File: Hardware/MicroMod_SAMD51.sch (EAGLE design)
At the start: 17 parts, among them J2 MICROMOD-2222, U1 W25QXX6X5, U2 ATSAMD51J20A-A, Y1 32.768kHz

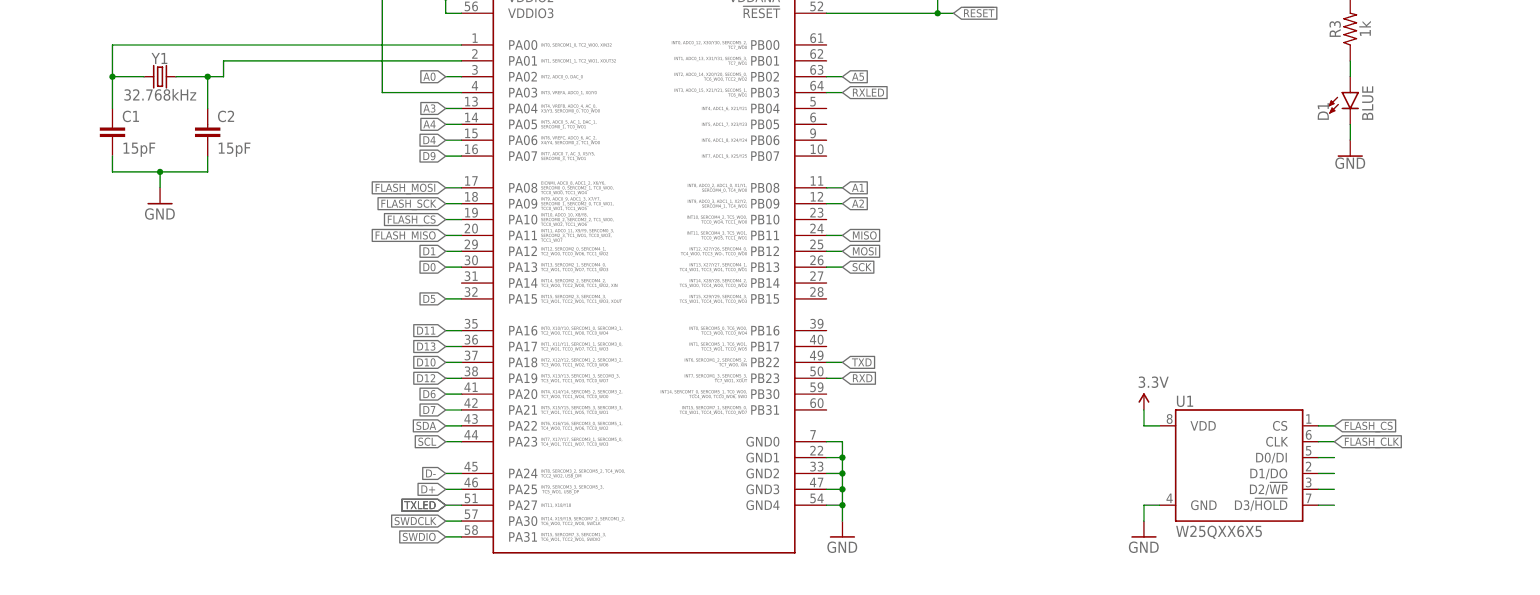
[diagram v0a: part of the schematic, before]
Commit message: Adds notes for quad spi, spi, and analog pins to schematic
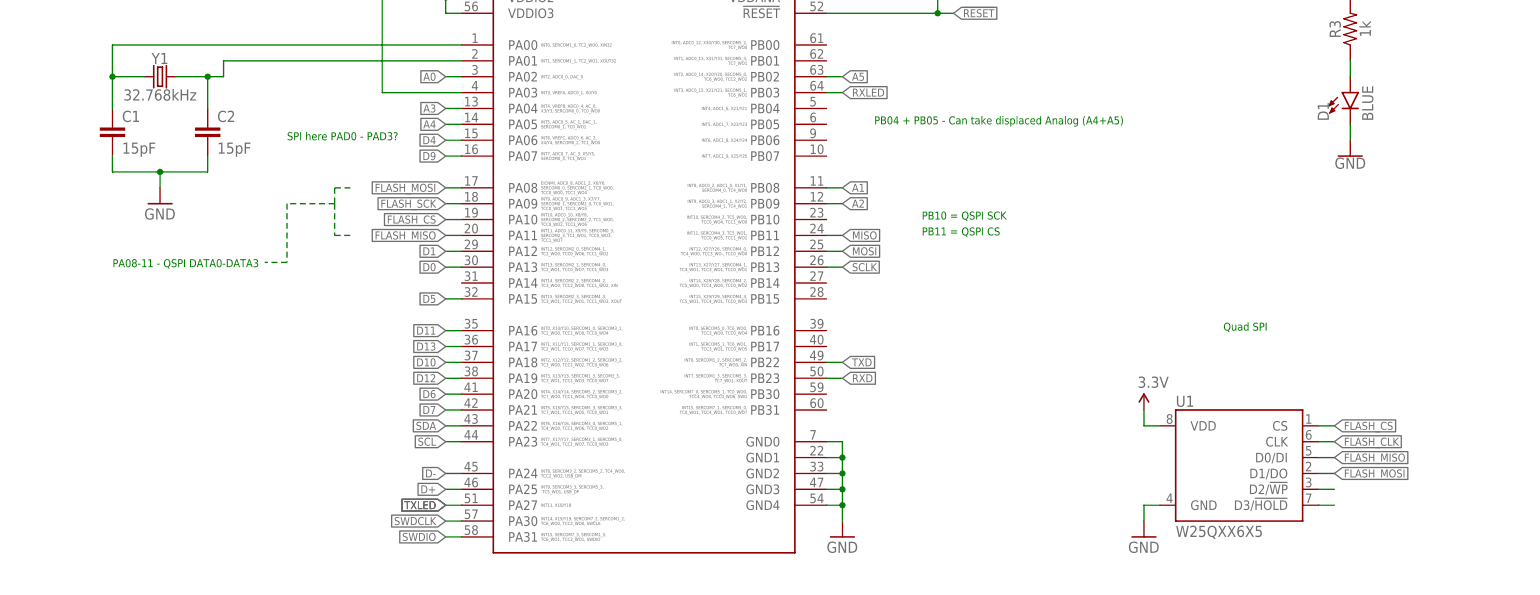
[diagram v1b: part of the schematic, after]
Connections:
- removed net N$4: U1.D0/DI
- removed net N$5: U1.D1/DO
- removed net SCK: U2.PB13
- net FLASH_MISO: now also U1.D0/DI
- net FLASH_MOSI: now also U1.D1/DO
- net SCLK: now also U2.PB13
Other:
- note added: "PA08-11 - QSPI DATA0-DATA3"
- note added: "PB04 + PB05 - Can take displaced Analog (A4+A5)"
- note added: "PB10 = QSPI SCK"
- note added: "PB11 = QSPI CS"
- note added: "Quad SPI"
- note added: "SPI here PAD0 - PAD3?"
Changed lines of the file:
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@@
 <wire x1="274.32" y1="279.4" x2="274.32" y2="111.76" width="0.1524" layer="97" style="longdash"/>
 <wire x1="274.32" y1="111.76" x2="431.8" y2="111.76" width="0.1524" layer="97" style="longdash"/>
+<text x="210.82" y="190.5" size="1.27" layer="91">Quad SPI</text>
+<text x="162.56" y="208.28" size="1.27" layer="91">PB10 = QSPI SCK</text>
+<text x="162.56" y="205.74" size="1.27" layer="91">PB11 = QSPI CS</text>
+<text x="33.02" y="200.66" size="1.27" layer="91">PA08-11 - QSPI DATA0-DATA3</text>
+<text x="60.96" y="220.98" size="1.27" layer="91">SPI here PAD0 - PAD3?</text>
+<text x="154.94" y="223.52" size="1.27" layer="91">PB04 + PB05 - Can take displaced Analog (A4+A5)</text>
 </plain>
 <instances>
@@
 <label x="86.36" y="213.36" size="1.27" layer="95" font="vector" rot="R180" xref="yes"/>
 </segment>
+<segment>
+<pinref part="U1" gate="U1" pin="D1/DO"/>
+<wire x1="226.06" y1="167.64" x2="228.6" y2="167.64" width="0.1524" layer="91"/>
+<label x="228.6" y="167.64" size="1.27" layer="95" xref="yes"/>
+</segment>
 </net>
 <net name="VCC" class="0">
@@
 </segment>
 </net>
-<net name="SCK" class="0">
-<segment>
-<pinref part="U2" gate="G$1" pin="PB13"/>
-<wire x1="147.32" y1="200.66" x2="149.86" y2="200.66" width="0.1524" layer="91"/>
-<label x="149.86" y="200.66" size="1.27" layer="95" xref="yes"/>
-</segment>
-</net>
 <net name="MOSI" class="0">
 <segment>
@@
 <label x="86.36" y="205.74" size="1.27" layer="95" font="vector" rot="R180" xref="yes"/>
 </segment>
+<segment>
+<pinref part="U1" gate="U1" pin="D0/DI"/>
+<wire x1="226.06" y1="170.18" x2="228.6" y2="170.18" width="0.1524" layer="91"/>
+<label x="228.6" y="170.18" size="1.27" layer="95" xref="yes"/>
+</segment>
 </net>
 <net name="LED_BUILTIN" class="0">
@@
 <label x="375.92" y="246.38" size="1.27" layer="95" xref="yes"/>
 </segment>
+<segment>
+<pinref part="U2" gate="G$1" pin="PB13"/>
+<wire x1="147.32" y1="200.66" x2="149.86" y2="200.66" width="0.1524" layer="91"/>
+<label x="149.86" y="200.66" size="1.27" layer="95" xref="yes"/>
+</segment>
 </net>
 <net name="!CS" class="0">
@@
 </segment>
 </net>
-<net name="N$4" class="0">
-<segment>
-<pinref part="U1" gate="U1" pin="D0/DI"/>
-<wire x1="226.06" y1="170.18" x2="228.6" y2="170.18" width="0.1524" layer="91"/>
-</segment>
-</net>
-<net name="N$5" class="0">
-<segment>
-<pinref part="U1" gate="U1" pin="D1/DO"/>
-<wire x1="226.06" y1="167.64" x2="228.6" y2="167.64" width="0.1524" layer="91"/>
-</segment>
-</net>
 <net name="N$6" class="0">
 <segment>
@@
 </segment>
 </net>
+<net name="N$2" class="0">
+<segment>
+<wire x1="71.12" y1="213.36" x2="68.58" y2="213.36" width="0.2032" layer="91" style="dashdot"/>
+<wire x1="68.58" y1="213.36" x2="68.58" y2="210.82" width="0.2032" layer="91" style="dashdot"/>
+<wire x1="68.58" y1="210.82" x2="68.58" y2="205.74" width="0.2032" layer="91" style="dashdot"/>
+<wire x1="68.58" y1="205.74" x2="71.12" y2="205.74" width="0.2032" layer="91" style="dashdot"/>
+<wire x1="68.58" y1="210.82" x2="60.96" y2="210.82" width="0.2032" layer="91" style="dashdot"/>
+<wire x1="60.96" y1="210.82" x2="60.96" y2="201.422" width="0.2032" layer="91" style="dashdot"/>
+<wire x1="60.96" y1="201.422" x2="57.404" y2="201.422" width="0.2032" layer="91" style="dashdot"/>
+</segment>
+</net>

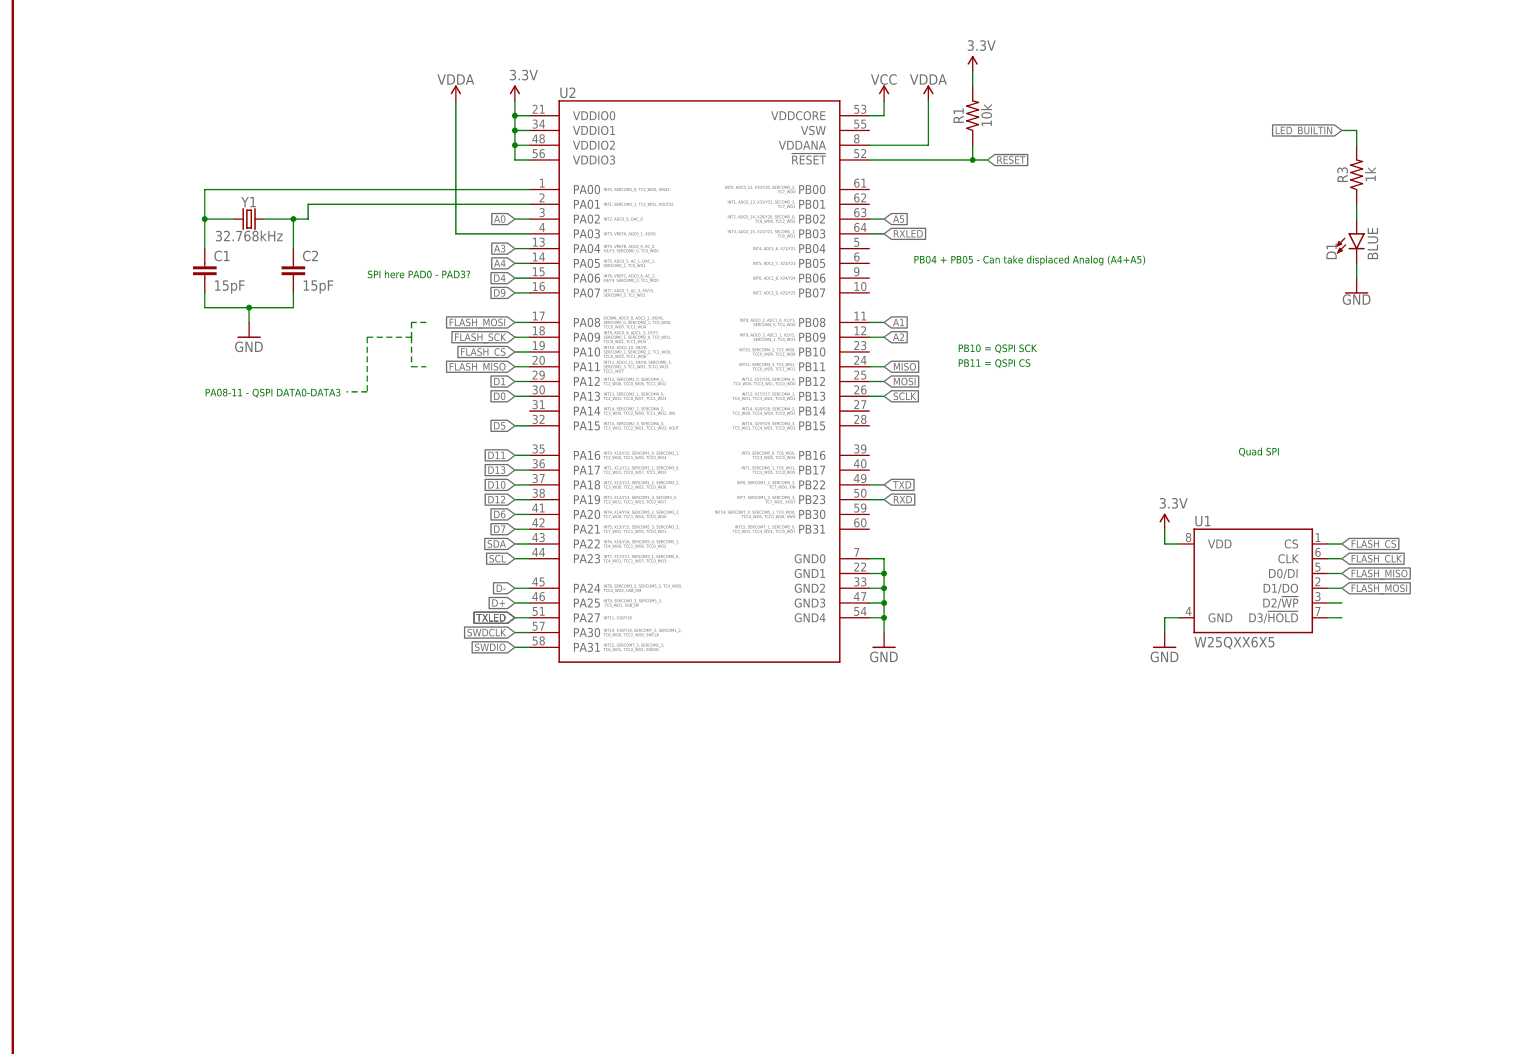
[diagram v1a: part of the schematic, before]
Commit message: Adds decoupling caps, adds I2S, and moves analog and digital pins
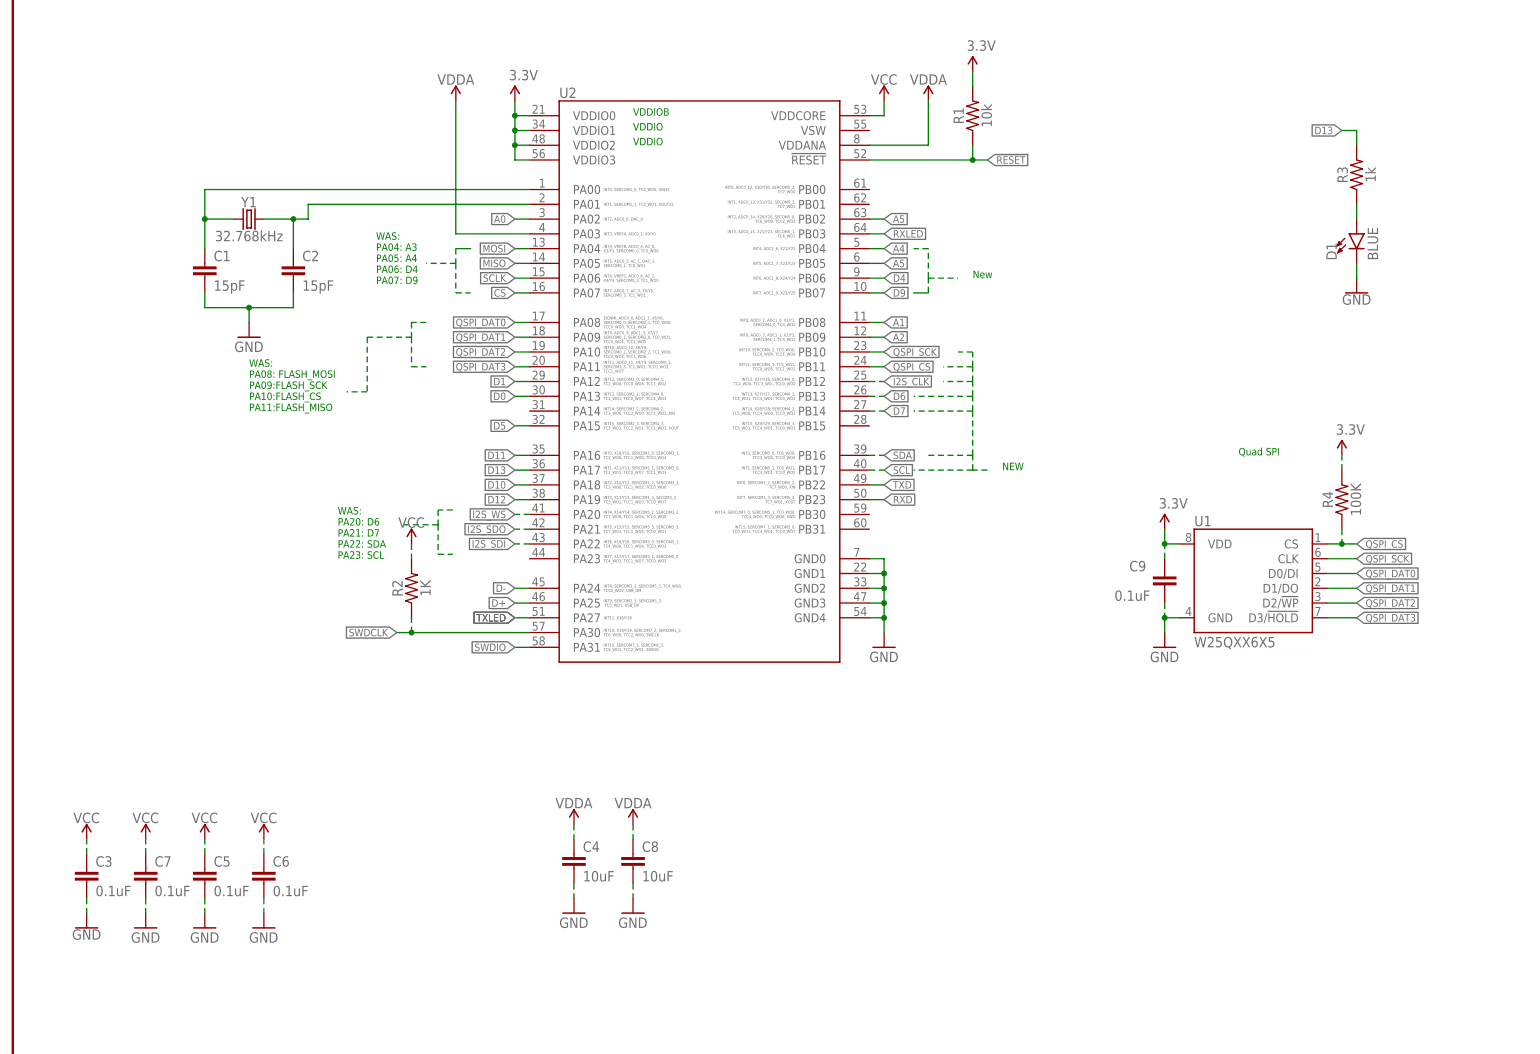
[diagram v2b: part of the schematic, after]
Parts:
- added C3, C5, C6, C7, C9: 0.1uF, SparkFun-Capacitors:0.1UF-0402-10V-10%-X7R
- added C4, C8: 10uF, SparkFun-Capacitors:10UF-0402T-6.3V-20%
- added R2: 1K, SparkFun-Resistors:1KOHM-0402-1/16W-1%
- added R4: 100K, SparkFun-Resistors:100KOHM-0402-1/16W-1%
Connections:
- removed net A3: U2.PA04
- removed net FLASH_CLK: U1.CLK
- removed net FLASH_CS: U1.CS, U2.PA10
- removed net FLASH_MISO: U1.D0/DI, U2.PA11
- removed net FLASH_MOSI: U1.D1/DO, U2.PA08
- removed net FLASH_SCK: U2.PA09
- removed net LED_BUILTIN: R3.2
- removed net N$6: U1.D2/!WP!
- removed net N$7: U1.D3/!HOLD!
- new net CS: U2.PA07
- new net I2S_CLK: U2.PB12
- new net I2S_SDI: U2.PA22
- new net I2S_SDO: U2.PA21
- new net I2S_WS: U2.PA20
- new net QSPI_CS: R4.1, U1.CS, U2.PB11
- new net QSPI_DAT0: U1.D0/DI, U2.PA08
- new net QSPI_DAT1: U1.D1/DO, U2.PA09
- new net QSPI_DAT2: U1.D2/!WP!, U2.PA10
- new net QSPI_DAT3: U1.D3/!HOLD!, U2.PA11
- new net QSPI_SCK: U1.CLK, U2.PB10
- net 3.3V: now also C9.1, R4.2
- net A4: now also U2.PB04; no longer U2.PA05
- net A5: now also U2.PB05
- net D13: now also R3.2
- net D4: now also U2.PB06; no longer U2.PA06
- net D6: now also U2.PB13; no longer U2.PA20
- net D7: now also U2.PB14; no longer U2.PA21
- net D9: now also U2.PB07; no longer U2.PA07
- net GND: now also C3.2, C4.2, C5.2, C6.2, C7.2, C8.2, C9.2
- net MISO: now also U2.PA05; no longer U2.PB11
- net MOSI: now also U2.PA04; no longer U2.PB12
- net SCL: now also U2.PB17; no longer U2.PA23
- net SCLK: now also U2.PA06; no longer U2.PB13
- net SDA: now also U2.PB16; no longer U2.PA22
- net SWDCLK: now also R2.1
- net VCC: now also C3.1, C5.1, C6.1, C7.1, R2.2
- net VDDA: now also C4.1, C8.1
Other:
- note added: "NEW"
- note added: "New"
- note added: "VDDIO"
- note added: "VDDIOB"
- note added: "WAS: PA04: A3 PA05: A4 PA06: D4 PA07: D9"
- note added: "WAS: PA08: FLASH_MOSI PA09:FLASH_SCK PA10:FLASH_CS PA11:FLASH_MISO"
- note added: "WAS: PA20: D6 PA21: D7 PA22: SDA PA23: SCL"
- note removed: "PA08-11 - QSPI DATA0-DATA3"
- note removed: "PB04 + PB05 - Can take displaced Analog (A4+A5)"
- note removed: "PB10 = QSPI SCK"
- note removed: "PB11 = QSPI CS"
- note removed: "SPI here PAD0 - PAD3?"

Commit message: Fixes schematic - adds second i2c, adds additional digital pins, and adds PWM pins
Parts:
- added C10: 0.1uF, SparkFun-Capacitors:0.1UF-0402-6.3V-10%-X7R
- added C11: 4.7uF, SparkFun-Capacitors:4.7UF-0402_TIGHT-6.3V-20%-X5R
- added L1: (no value), SparkFun-Coils:INDUCTORFB-30OHM
- added S1: MOMENTARY-SWITCH-SPST-SMD-4.6X2.8MM, SparkFun-Switches:MOMENTARY-SWITCH-SPST-SMD-4.6X2.8MM
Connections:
- net PWM1 renamed A3
- removed net !BOOT: J2.!BOOT!
- removed net A4: U2.PB04
- removed net A5: U2.PB02, U2.PB05
- removed net CS: U2.PA07
- removed net CTS1: J2.CTS1
- removed net GPIO0: J2.G0/BUS0
- removed net GPIO1: J2.G1/BUS1
- removed net GPIO10: J2.G10/ADC_D+/CAM_VSYNC
- removed net GPIO11: J2.G11
- removed net GPIO2: J2.G2/BUS2
- removed net GPIO3: J2.G3/BUS3
- removed net GPIO4: J2.G4/BUS4
- removed net GPIO5: J2.G5/BUS5
- removed net GPIO6: J2.G6/BUS6
- removed net GPIO7: J2.G7/BUS7
- removed net GPIO8: J2.G8
- removed net GPIO9: J2.G9/ADC_D-/CAM_HSYNC
- removed net PWM0: J2.PWM0
- removed net RTS1: J2.RTS1
- removed net RX1: J2.RX1
- removed net RX2: J2.RX2
- removed net RXD: U2.PB23
- removed net RXLED: U2.PB03
- removed net SDIO_CLK: J2.SDIO_CLK/SCK1
- removed net SDIO_CMD: J2.SDIO_CMD/MOSI1
- removed net SDIO_DATA: J2.SDIO_DATA0/MISO1
- removed net SDIO_DATA1: J2.SDIO_DATA1
- removed net SDIO_DATA2: J2.SDIO_DATA2
- removed net SDIO_DATA3: J2.SDIO_DATA3
- removed net SWDCLK: R2.1, U2.PA30
- removed net TX1: J2.TX1
- removed net TX2: J2.TX2
- removed net TXD: U2.PB22
- removed net TXLED: U2.PA27
- removed net USB_D+: J2.USB_D+
- removed net USB_D-: J2.USB_D-
- new net !CS1: J2.SDIO_DATA1, U2.PB03
- new net CAN_RXI: J2.CAN-RX, U2.PB15
- new net CAN_TXO: J2.CAN-TX, U2.PB14
- new net D2: J2.G0/BUS0, U2.PA19
- new net D3: J2.G1/BUS1, U2.PB06
- new net D8: J2.G6/BUS6, U2.PA16
- new net MISO1: J2.SDIO_DATA0/MISO1, U2.PB01
- new net MOSI1: J2.SDIO_CMD/MOSI1, U2.PB00
- new net RXI: J2.RX1, U2.PB23
- new net SCL1: J2.I2C_SCL1, U2.PA12
- new net SCLK1: J2.SDIO_CLK/SCK1, U2.PB02
- new net SDA1: J2.I2C_SDA1, U2.PA13
- new net TXO: J2.TX1, U2.PB22
- net !CS: now also U2.PA07
- net !RESET: now also S1.1
- net 3.3V: now also C3.1, C5.1, C6.1, C7.1, L1.1, R2.2
- net A2: now also J2.PWM0
- net D+: now also J2.USB_D+
- net D-: now also J2.USB_D-
- net D0: now also U2.PA14; no longer U2.PA13
- net D1: now also U2.PA27; no longer U2.PA12
- net D10: now also J2.G8, U2.PB05; no longer U2.PA18
- net D11: now also J2.G9/ADC_D-/CAM_HSYNC, U2.PB30; no longer U2.PA16
- net D12: now also J2.G10/ADC_D+/CAM_VSYNC, U2.PB31; no longer U2.PA19
- net D4: now also J2.G2/BUS2, U2.PA15; no longer U2.PB06
- net D5: now also J2.G3/BUS3, U2.PB13; no longer U2.PA15
- net D6: now also J2.G4/BUS4, U2.PB07; no longer U2.PB13
- net D7: now also J2.G5/BUS5, U2.PA18; no longer U2.PB14
- net D9: now also J2.G7/BUS7, U2.PB04; no longer U2.PB07
- net GND: now also C10.2, C11.2, S1.2
- net I2S_CLK: now also J2.AUD_BCLK
- net I2S_SDI: now also J2.AUD_IN/CAM_PCLK
- net I2S_SDO: now also J2.AUD_OUT/CAM_MCLK
- net I2S_WS: now also J2.AUD_LRCLK
- net SWDCK: now also R2.1, U2.PA30
- net VCC: now also C10.1, C11.1; no longer C3.1, C5.1, C6.1, C7.1, R2.2
- net VDDA: now also L1.2
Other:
- note added: "Flash Memory - 128MB"
- note added: "Microcontroller - SAMD51"
- note added: "PIN 21"
- note added: "PIN 34"
- note added: "PIN 48"
- note added: "PIN 53"
- note added: "PIN 56"
- note added: "PIN 8"
- note added: "Reset Switch and Stat LED"
- note added: "WAS: PA19: D12 PA20: D6 PA21: D7 PA22: SDA PA23: SCL"
- note removed: "Quad SPI"
- note removed: "WAS: PA20: D6 PA21: D7 PA22: SDA PA23: SCL"
- moved on the sheet: C1, C2, C3, C4, C5, C6, C7, C8, C9, D1, R1, R2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
